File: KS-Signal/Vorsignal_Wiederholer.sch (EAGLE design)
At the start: 24 parts, among them IC1 ATTINY44SSU, Q1 IRLML5203, X1 SSW-106-02-S-S-RA, X2 TSW-106-02-S-S-RA

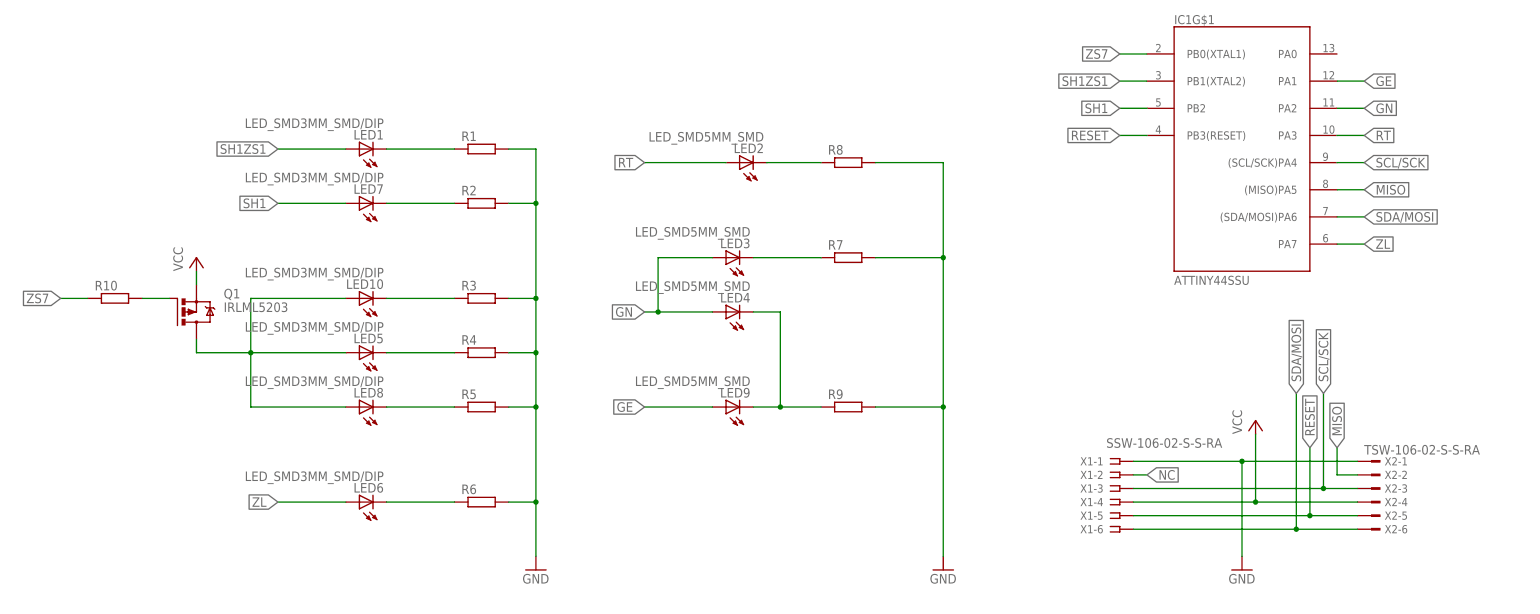
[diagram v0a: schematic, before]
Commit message: Vorsignale fertiggestellt
- Vorsignalschirme fertiggestellt
- Platinengrößen angepasst
-> Achtung: Stecker und Pinbelegung unterschiedlich zwischen den beiden Vorsignaltypen
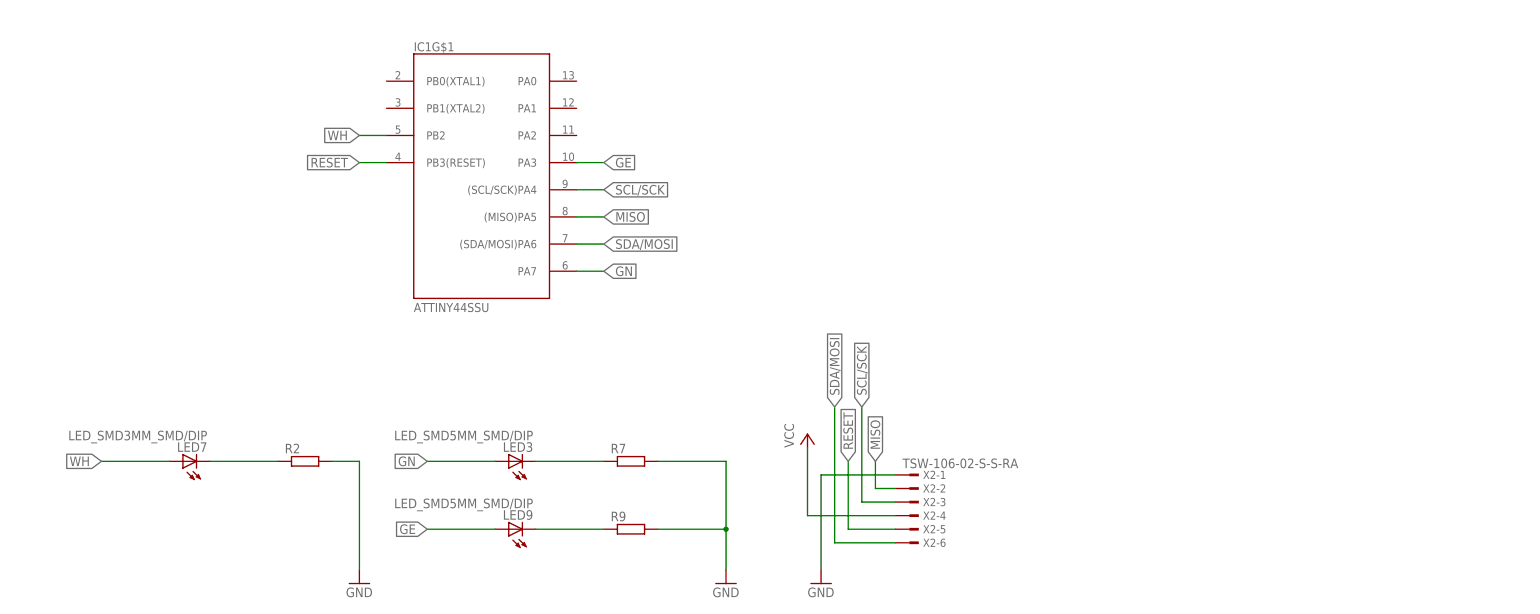
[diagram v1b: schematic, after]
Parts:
- removed LED1, LED10, LED5, LED6, LED8: LED_SMD3MM_SMD/DIP, LEDFLATTOP:LED_SMD3MM_SMD/DIP
- removed LED2, LED4: LED_SMD5MM_SMD, LEDFLATTOP:LED_SMD5MM_SMD
- removed Q1: IRLML5203, transistor-power:IRLML5203
- removed R1, R10, R3, R4, R5, R6, R8: (no value), rcl:R-EU_R0603
- removed X1: SSW-106-02-S-S-RA, con-samtec:SSW-106-02-S-S-RA
- LED3, LED9: value LED_SMD5MM_SMD -> LED_SMD5MM_SMD/DIP; device LEDFLATTOP:LED_SMD5MM_SMD -> LEDFLATTOP:LED_SMD5MM_SMD/DIP
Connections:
- net SH1 renamed WH
- removed net N$10: LED10.A, LED5.A, LED8.A, Q1.D
- removed net N$11: Q1.G, R10.2
- removed net N$2: LED6.C, R6.1
- removed net N$3: LED8.C, R5.1
- removed net N$4: LED5.C, R4.1
- removed net N$5: LED10.C, R3.1
- removed net N$7: LED1.C, R1.1
- removed net N$9: LED2.C, R8.1
- removed net NC: X1-2.1
- removed net RT: IC1G$1.PA3, LED2.A
- removed net SH1ZS1: IC1G$1.PB1(XTAL2), LED1.A
- removed net ZL: IC1G$1.PA7, LED6.A
- removed net ZS7: IC1G$1.PB0(XTAL1), R10.1
- net GE: now also IC1G$1.PA3; no longer IC1G$1.PA1
- net GN: now also IC1G$1.PA7; no longer IC1G$1.PA2, LED4.A
- net GND: no longer R1.2, R3.2, R4.2, R5.2, R6.2, R8.2, X1-1.1
- net N$1: no longer LED4.C
- net RESET: no longer X1-5.1
- net SCL/SCK: no longer X1-3.1
- net SDA/MOSI: no longer X1-6.1
- net VCC: no longer Q1.S, X1-4.1
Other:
- moved on the sheet: IC1G$1, LED3, LED7, LED9, R2, R7, R9, X2-1, X2-2, X2-3, X2-4, X2-5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
